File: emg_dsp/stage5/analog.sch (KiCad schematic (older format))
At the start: 37 parts, among them U43 OMNETICS_36

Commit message: working on stage5 already -- will it be tight?
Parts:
- removed TP?: MXA, TP, symbol TP
- removed TP?: MXB, TP, symbol TP
- U26: renamed from U?; footprint (none) -> SC-70-5
- gave numbers to parts that had none: 28
- renumbered C68 to C46, C70 to C49, C76 to C53, L8 to L7, TP174 to TP29, U43 to U24
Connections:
- net E1: now also U24.17 (in16); no longer U24.2 (in1)
- net E10: now also U24.8 (in7); no longer U24.11 (in10)
- net E11: now also U24.7 (in6); no longer U24.12 (in11)
- net E12: now also U24.6 (in5); no longer U24.13 (in12)
- net E13: now also U24.5 (in4); no longer U24.14 (in13)
- net E14: now also U24.4 (in3); no longer U24.15 (in14)
- net E15: now also U24.3 (in2); no longer U24.16 (in15)
- net E16: now also U24.2 (in1); no longer U24.17 (in16)
- net E2: now also U24.16 (in15); no longer U24.3 (in2)
- net E3: now also U24.15 (in14); no longer U24.4 (in3)
- net E4: now also U24.14 (in13); no longer U24.5 (in4)
- net E5: now also U24.13 (in12); no longer U24.6 (in5)
- net E6: now also U24.12 (in11); no longer U24.7 (in6)
- net E7: now also U24.11 (in10); no longer U24.8 (in7)
- net E8: now also U24.10 (in9); no longer U24.9 (in8)
- net E9: now also U24.9 (in8); no longer U24.10 (in9)

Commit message: routing stage5.
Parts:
- removed R45, R51: 3.3k, 0402, symbol R
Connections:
- net E1: now also U25.28 (in15); no longer U25.3 (in0)
- net E10: now also U25.37 (in6); no longer U25.34 (in9)
- net E11: now also U25.38 (in5); no longer U25.33 (in10)
- net E12: now also U25.39 (in4); no longer U25.32 (in11)
- net E13: now also U25.40 (in3); no longer U25.31 (in12)
- net E14: now also U25.1 (in2); no longer U25.30 (in13)
- net E15: now also U25.2 (in1); no longer U25.29 (in14)
- net E16: now also U25.3 (in0); no longer U25.28 (in15)
- net E17: now also U29.28 (in15); no longer U29.3 (in0)
- net E18: now also U29.29 (in14); no longer U29.2 (in1)
- net E19: now also U29.30 (in13); no longer U29.1 (in2)
- net E2: now also U25.29 (in14); no longer U25.2 (in1)
- net E20: now also U29.31 (in12); no longer U29.40 (in3)
- net E21: now also U29.32 (in11); no longer U29.39 (in4)
- net E22: now also U29.33 (in10); no longer U29.38 (in5)
- net E23: now also U29.34 (in9); no longer U29.37 (in6)
- net E24: now also U29.35 (in8); no longer U29.36 (in7)
- net E25: now also U29.36 (in7); no longer U29.35 (in8)
- net E26: now also U29.37 (in6); no longer U29.34 (in9)
- net E27: now also U29.38 (in5); no longer U29.33 (in10)
- net E28: now also U29.39 (in4); no longer U29.32 (in11)
- net E29: now also U29.40 (in3); no longer U29.31 (in12)
- net E3: now also U25.30 (in13); no longer U25.1 (in2)
- net E30: now also U29.1 (in2); no longer U29.30 (in13)
- net E31: now also U29.2 (in1); no longer U29.29 (in14)
- net E32: now also U29.3 (in0); no longer U29.28 (in15)
- net E4: now also U25.31 (in12); no longer U25.40 (in3)
- net E5: now also U25.32 (in11); no longer U25.39 (in4)
- net E6: now also U25.33 (in10); no longer U25.38 (in5)
- net E7: now also U25.34 (in9); no longer U25.37 (in6)
- net E8: now also U25.35 (in8); no longer U25.36 (in7)
- net E9: now also U25.36 (in7); no longer U25.35 (in8)
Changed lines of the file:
@@
-EESchema Schematic File Version 2  date Tue 29 Jun 2010 08:13:18 PM EDT
+EESchema Schematic File Version 2  date Wed 30 Jun 2010 05:27:19 PM EDT
 LIBS:power
 LIBS:device
@@
 Text HLabel 9550 2350 2    60   Input ~ 0
 _reset
+Text Label 7150 1100 0    60   ~ 0
+E32
+Text Label 7150 1200 0    60   ~ 0
+E31
+Text Label 7150 1300 0    60   ~ 0
+E30
+Text Label 7150 1400 0    60   ~ 0
+E29
+Text Label 7150 1500 0    60   ~ 0
+E28
+Text Label 7150 1600 0    60   ~ 0
+E27
+Text Label 7150 1700 0    60   ~ 0
+E26
+Text Label 7150 1800 0    60   ~ 0
+E25
+Text Label 7150 1900 0    60   ~ 0
+E24
+Text Label 7150 2000 0    60   ~ 0
+E23
+Text Label 7150 2100 0    60   ~ 0
+E22
+Text Label 7150 2200 0    60   ~ 0
+E21
+Text Label 7150 2300 0    60   ~ 0
+E20
+Text Label 7150 2400 0    60   ~ 0
+E19
+Text Label 7150 2500 0    60   ~ 0
+E18
 Text Label 7150 2600 0    60   ~ 0
-E32
-Text Label 7150 2500 0    60   ~ 0
-E31
-Text Label 7150 2400 0    60   ~ 0
-E30
-Text Label 7150 2300 0    60   ~ 0
-E29
-Text Label 7150 2200 0    60   ~ 0
-E28
-Text Label 7150 2100 0    60   ~ 0
-E27
-Text Label 7150 2000 0    60   ~ 0
-E26
-Text Label 7150 1900 0    60   ~ 0
-E25
-Text Label 7150 1800 0    60   ~ 0
-E24
-Text Label 7150 1700 0    60   ~ 0
-E23
-Text Label 7150 1600 0    60   ~ 0
-E22
-Text Label 7150 1500 0    60   ~ 0
-E21
-Text Label 7150 1400 0    60   ~ 0
-E20
-Text Label 7150 1300 0    60   ~ 0
-E19
-Text Label 7150 1200 0    60   ~ 0
-E18
-Text Label 7150 1100 0    60   ~ 0
 E17
 $Comp
@@
 F 2 "0402" V 9400 2150 60  0000 C CNN
 	1    9400 1800
-	0    1    1    0
-$EndComp
-$Comp
-L R R51
-U 1 1 4C2A3384
-P 9400 1950
-F 0 "R51" V 9480 1950 50  0000 C CNN
-F 1 "3.3k" V 7500 550 50  0000 C CNN
-F 2 "0402" V 9400 2300 60  0000 C CNN
-	1    9400 1950
 	0    1    1    0
 $EndComp
@@
 $EndComp
 $Comp
-L R R45
-U 1 1 4C2A306D
-P 5450 1950
-F 0 "R45" V 5530 1950 50  0000 C CNN
-F 1 "3.3k" V 3550 550 50  0000 C CNN
-F 2 "0402" V 5450 2300 60  0000 C CNN
-	1    5450 1950
-	0    1    1    0
-$EndComp
-$Comp
 L R R44
 U 1 1 4C2A303D
@@
 	1    0    0    -1
 $EndComp
+Text Label 3200 1100 0    60   ~ 0
+E16
+Text Label 3200 1200 0    60   ~ 0
+E15
+Text Label 3200 1300 0    60   ~ 0
+E14
+Text Label 3200 1400 0    60   ~ 0
+E13
+Text Label 3200 1500 0    60   ~ 0
+E12
+Text Label 3200 1600 0    60   ~ 0
+E11
+Text Label 3200 1700 0    60   ~ 0
+E10
+Text Label 3200 1800 0    60   ~ 0
+E9
+Text Label 3200 1900 0    60   ~ 0
+E8
+Text Label 3200 2000 0    60   ~ 0
+E7
+Text Label 3200 2100 0    60   ~ 0
+E6
+Text Label 3200 2200 0    60   ~ 0
+E5
+Text Label 3200 2300 0    60   ~ 0
+E4
+Text Label 3200 2400 0    60   ~ 0
+E3
+Text Label 3200 2500 0    60   ~ 0
+E2
 Text Label 3200 2600 0    60   ~ 0
-E16
-Text Label 3200 2500 0    60   ~ 0
-E15
-Text Label 3200 2400 0    60   ~ 0
-E14
-Text Label 3200 2300 0    60   ~ 0
-E13
-Text Label 3200 2200 0    60   ~ 0
-E12
-Text Label 3200 2100 0    60   ~ 0
-E11
-Text Label 3200 2000 0    60   ~ 0
-E10
-Text Label 3200 1900 0    60   ~ 0
-E9
-Text Label 3200 1800 0    60   ~ 0
-E8
-Text Label 3200 1700 0    60   ~ 0
-E7
-Text Label 3200 1600 0    60   ~ 0
-E6
-Text Label 3200 1500 0    60   ~ 0
-E5
-Text Label 3200 1400 0    60   ~ 0
-E4
-Text Label 3200 1300 0    60   ~ 0
-E3
-Text Label 3200 1200 0    60   ~ 0
-E2
-Text Label 3200 1100 0    60   ~ 0
 E1
 $Comp

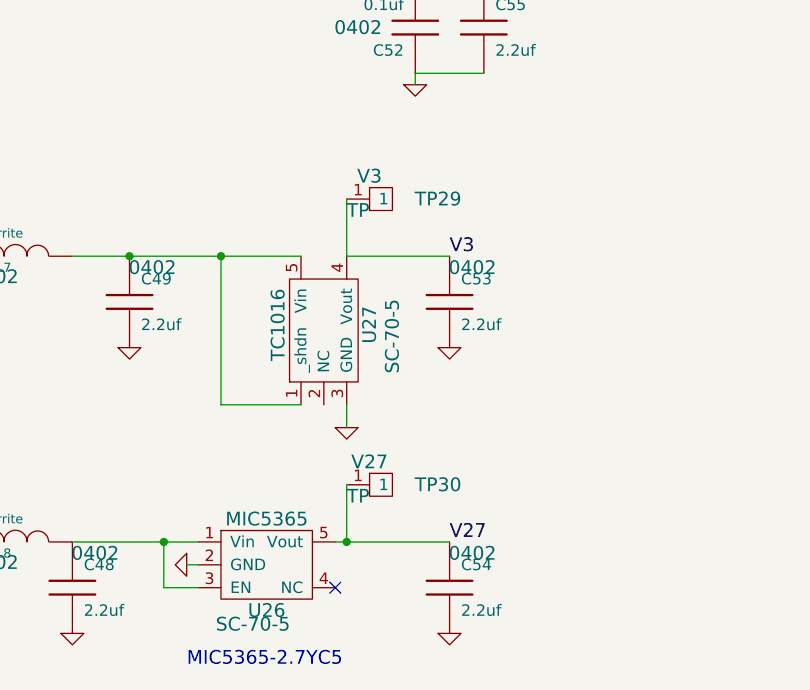
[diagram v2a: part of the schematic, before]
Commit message: board nearing completion - at least with routing! seems to be a bug in the netlist, though -- have to check it out.
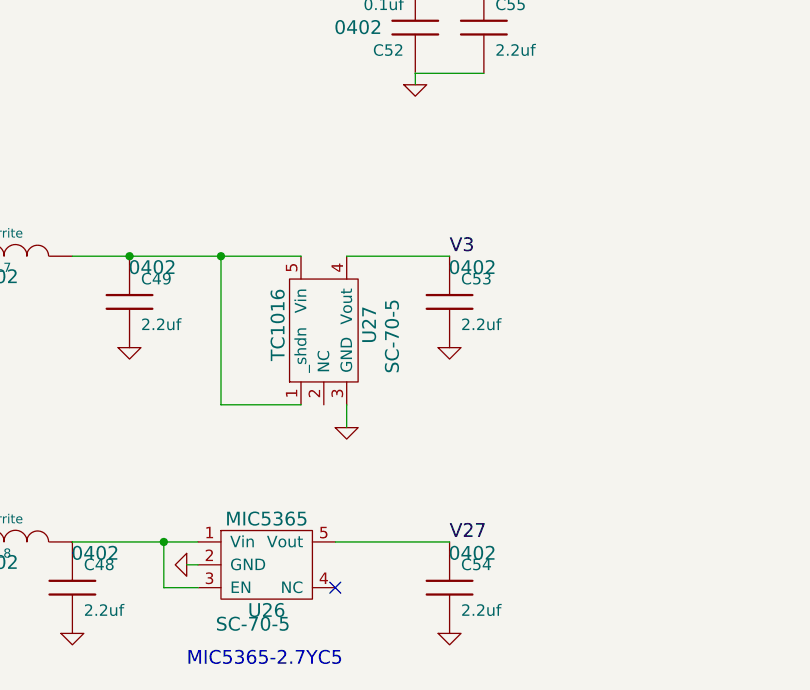
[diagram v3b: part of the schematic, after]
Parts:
- removed TP29: V3, TP, symbol TP
- removed TP30: V27, TP, symbol TP
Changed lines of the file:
@@
-EESchema Schematic File Version 2  date Wed 30 Jun 2010 05:27:19 PM EDT
+EESchema Schematic File Version 2  date Thu 01 Jul 2010 08:06:38 PM EDT
 LIBS:power
 LIBS:device
@@
 Sheet 2 2
 Title "Stage 4 / Copyright 2010 Timothy L Hanson "
-Date "30 jun 2010"
+Date "2 jul 2010"
 Rev ""
 Comp "This design is free: redistribute or modify under the GPL v. 3 or later"
@@
 Wire Wire Line
 	3050 4650 3050 4500
-Connection ~ 4850 5900
 Wire Wire Line
 	4800 5900 5300 5900
@@
 Wire Wire Line
 	5300 4650 4850 4650
-Wire Wire Line
-	4850 4650 4850 4400
-Wire Wire Line
-	4850 5900 4850 5650
 Wire Wire Line
 	3050 5900 3050 5750
@@
 $EndComp
 $Comp
-L GND #PWR0119
+L GND #PWR0121
 U 1 1 4C2A3423
 P 8050 650
-F 0 "#PWR0119" H 8050 650 30  0001 C CNN
+F 0 "#PWR0121" H 8050 650 30  0001 C CNN
 F 1 "GND" H 8050 580 30  0001 C CNN
 	1    8050 650
@@
 $EndComp
 $Comp
-L GND #PWR0120
+L GND #PWR0122
 U 1 1 4C2A338B
 P 7300 2850
-F 0 "#PWR0120" H 7300 2850 30  0001 C CNN
+F 0 "#PWR0122" H 7300 2850 30  0001 C CNN
 F 1 "GND" H 7300 2780 30  0001 C CNN
 	1    7300 2850
@@
 $EndComp
 $Comp
-L GND #PWR0121
+L GND #PWR0123
 U 1 1 4C2A338A
 P 8850 3000
-F 0 "#PWR0121" H 8850 3000 30  0001 C CNN
+F 0 "#PWR0123" H 8850 3000 30  0001 C CNN
 F 1 "GND" H 8850 2930 30  0001 C CNN
 	1    8850 3000
@@
 $EndComp
 $Comp
-L GND #PWR0122
+L GND #PWR0124
 U 1 1 4C2A3388
 P 9300 3050
-F 0 "#PWR0122" H 9300 3050 30  0001 C CNN
+F 0 "#PWR0124" H 9300 3050 30  0001 C CNN
 F 1 "GND" H 9300 2980 30  0001 C CNN
 	1    9300 3050
@@
 $EndComp
 $Comp
-L GND #PWR0123
+L GND #PWR0125
 U 1 1 4C2A3386
 P 9100 3900
-F 0 "#PWR0123" H 9100 3900 30  0001 C CNN
+F 0 "#PWR0125" H 9100 3900 30  0001 C CNN
 F 1 "GND" H 9100 3830 30  0001 C CNN
 	1    9100 3900
@@
 $EndComp
 $Comp
-L GND #PWR0124
+L GND #PWR0126
 U 1 1 4C2A3382
 P 9650 1800
-F 0 "#PWR0124" H 9650 1800 30  0001 C CNN
+F 0 "#PWR0126" H 9650 1800 30  0001 C CNN
 F 1 "GND" H 9650 1730 30  0001 C CNN
 	1    9650 1800
@@
 $EndComp
 $Comp
-L GND #PWR0125
+L GND #PWR0127
 U 1 1 4C2A3381
 P 9650 1950
-F 0 "#PWR0125" H 9650 1950 30  0001 C CNN
+F 0 "#PWR0127" H 9650 1950 30  0001 C CNN
 F 1 "GND" H 9650 1880 30  0001 C CNN
 	1    9650 1950
@@
 $EndComp
 $Comp
-L GND #PWR0126
+L GND #PWR0128
 U 1 1 4C2A337F
 P 9650 2100
-F 0 "#PWR0126" H 9650 2100 30  0001 C CNN
+F 0 "#PWR0128" H 9650 2100 30  0001 C CNN
 F 1 "GND" H 9650 2030 30  0001 C CNN
 	1    9650 2100
@@
 $EndComp
 $Comp
-L GND #PWR0127
+L GND #PWR0129
 U 1 1 4C2A337C
 P 8900 1800
-F 0 "#PWR0127" H 8900 1800 30  0001 C CNN
+F 0 "#PWR0129" H 8900 1800 30  0001 C CNN
 F 1 "GND" H 8900 1730 30  0001 C CNN
 	1    8900 1800
@@
 $EndComp
 $Comp
-L GND #PWR0128
+L GND #PWR0130
 U 1 1 4C2A337B
 P 8900 1250
-F 0 "#PWR0128" H 8900 1250 30  0001 C CNN
+F 0 "#PWR0130" H 8900 1250 30  0001 C CNN
 F 1 "GND" H 8900 1180 30  0001 C CNN
 	1    8900 1250
@@
 V3
 $Comp
-L GND #PWR0129
+L GND #PWR0131
 U 1 1 4C2A337A
 P 8900 2350
-F 0 "#PWR0129" H 8900 2350 30  0001 C CNN
+F 0 "#PWR0131" H 8900 2350 30  0001 C CNN
 F 1 "GND" H 8900 2280 30  0001 C CNN
 	1    8900 2350
@@
 $EndComp
 $Comp
-L GND #PWR0130
+L GND #PWR0132
 U 1 1 4C2A3379
 P 8100 3300
-F 0 "#PWR0130" H 8100 3300 30  0001 C CNN
+F 0 "#PWR0132" H 8100 3300 30  0001 C CNN
 F 1 "GND" H 8100 3230 30  0001 C CNN
 	1    8100 3300
@@
 NoConn ~ 3950 3100
 $Comp
-L GND #PWR0131
+L GND #PWR0133
 U 1 1 4C2A32DF
 P 4100 650
-F 0 "#PWR0131" H 4100 650 30  0001 C CNN
+F 0 "#PWR0133" H 4100 650 30  0001 C CNN
 F 1 "GND" H 4100 580 30  0001 C CNN
 	1    4100 650
@@
 $EndComp
 $Comp
-L GND #PWR0132
+L GND #PWR0134
 U 1 1 4C2A32D7
 P 4150 3300
-F 0 "#PWR0132" H 4150 3300 30  0001 C CNN
+F 0 "#PWR0134" H 4150 3300 30  0001 C CNN
 F 1 "GND" H 4150 3230 30  0001 C CNN
 	1    4150 3300
@@
 $EndComp
 $Comp
-L GND #PWR0133
+L GND #PWR0135
 U 1 1 4C2A32BF
 P 4950 2350
-F 0 "#PWR0133" H 4950 2350 30  0001 C CNN
+F 0 "#PWR0135" H 4950 2350 30  0001 C CNN
 F 1 "GND" H 4950 2280 30  0001 C CNN
 	1    4950 2350
@@
 V3
 $Comp
-L GND #PWR0134
+L GND #PWR0136
 U 1 1 4C2A3286
 P 4950 1250
-F 0 "#PWR0134" H 4950 1250 30  0001 C CNN
+F 0 "#PWR0136" H 4950 1250 30  0001 C CNN
 F 1 "GND" H 4950 1180 30  0001 C CNN
 	1    4950 1250
@@
 $EndComp
 $Comp
-L GND #PWR0135
+L GND #PWR0137
 U 1 1 4C2A3267
 P 4950 1800
-F 0 "#PWR0135" H 4950 1800 30  0001 C CNN
+F 0 "#PWR0137" H 4950 1800 30  0001 C CNN
 F 1 "GND" H 4950 1730 30  0001 C CNN
 	1    4950 1800
@@
 $EndComp
 $Comp
-L GND #PWR0136
+L GND #PWR0138
 U 1 1 4C2A3090
 P 5700 2100
-F 0 "#PWR0136" H 5700 2100 30  0001 C CNN
+F 0 "#PWR0138" H 5700 2100 30  0001 C CNN
 F 1 "GND" H 5700 2030 30  0001 C CNN
 	1    5700 2100
@@
 $EndComp
 $Comp
-L GND #PWR0137
+L GND #PWR0139
 U 1 1 4C2A3089
 P 5700 1950
-F 0 "#PWR0137" H 5700 1950 30  0001 C CNN
+F 0 "#PWR0139" H 5700 1950 30  0001 C CNN
 F 1 "GND" H 5700 1880 30  0001 C CNN
 	1    5700 1950
@@
 $EndComp
 $Comp
-L GND #PWR0138
+L GND #PWR0140
 U 1 1 4C2A3084
 P 5700 1800
-F 0 "#PWR0138" H 5700 1800 30  0001 C CNN
+F 0 "#PWR0140" H 5700 1800 30  0001 C CNN
 F 1 "GND" H 5700 1730 30  0001 C CNN
 	1    5700 1800
@@
 V27
 $Comp
-L VDD #PWR0139
+L VDD #PWR0141
 U 1 1 4C2A2EC5
 P 3050 5750
-F 0 "#PWR0139" H 3050 5850 30  0001 C CNN
+F 0 "#PWR0141" H 3050 5850 30  0001 C CNN
 F 1 "VDD" H 3050 5860 30  0000 C CNN
 	1    3050 5750
@@
 $EndComp
 $Comp
-L GND #PWR0140
+L GND #PWR0142
 U 1 1 4C2A2E8B
 P 5150 3900
-F 0 "#PWR0140" H 5150 3900 30  0001 C CNN
+F 0 "#PWR0142" H 5150 3900 30  0001 C CNN
 F 1 "GND" H 5150 3830 30  0001 C CNN
 	1    5150 3900
@@
 $EndComp
 $Comp
-L GND #PWR0141
+L GND #PWR0143
 U 1 1 4C2A2E11
 P 5350 3050
-F 0 "#PWR0141" H 5350 3050 30  0001 C CNN
+F 0 "#PWR0143" H 5350 3050 30  0001 C CNN
 F 1 "GND" H 5350 2980 30  0001 C CNN
 	1    5350 3050
@@
 $EndComp
 $Comp
-L GND #PWR0142
+L GND #PWR0144
 U 1 1 4C2A2DE8
 P 4900 3000
-F 0 "#PWR0142" H 4900 3000 30  0001 C CNN
+F 0 "#PWR0144" H 4900 3000 30  0001 C CNN
 F 1 "GND" H 4900 2930 30  0001 C CNN
 	1    4900 3000
@@
 $EndComp
 $Comp
-L GND #PWR0143
+L GND #PWR0145
 U 1 1 4C2A2DD8
 P 3350 2850
-F 0 "#PWR0143" H 3350 2850 30  0001 C CNN
+F 0 "#PWR0145" H 3350 2850 30  0001 C CNN
 F 1 "GND" H 3350 2780 30  0001 C CNN
 	1    3350 2850
@@
 $EndComp
 $Comp
-L GND #PWR0144
+L GND #PWR0146
 U 1 1 4C2A2B2E
 P 5300 6300
-F 0 "#PWR0144" H 5300 6300 30  0001 C CNN
+F 0 "#PWR0146" H 5300 6300 30  0001 C CNN
 F 1 "GND" H 5300 6230 30  0001 C CNN
 	1    5300 6300
@@
 $EndComp
 $Comp
-L GND #PWR0145
+L GND #PWR0147
 U 1 1 4C2A2B2C
 P 3650 6300
-F 0 "#PWR0145" H 3650 6300 30  0001 C CNN
+F 0 "#PWR0147" H 3650 6300 30  0001 C CNN
 F 1 "GND" H 3650 6230 30  0001 C CNN
 	1    3650 6300
@@
 $EndComp
 $Comp
-L GND #PWR0146
+L GND #PWR0148
 U 1 1 4C2A2B2B
 P 4150 6000
-F 0 "#PWR0146" H 4150 6000 30  0001 C CNN
+F 0 "#PWR0148" H 4150 6000 30  0001 C CNN
 F 1 "GND" H 4150 5930 30  0001 C CNN
 	1    4150 6000
@@
 $EndComp
 $Comp
-L GND #PWR0147
+L GND #PWR0149
 U 1 1 4C2A2B28
 P 3050 6300
-F 0 "#PWR0147" H 3050 6300 30  0001 C CNN
+F 0 "#PWR0149" H 3050 6300 30  0001 C CNN
 F 1 "GND" H 3050 6230 30  0001 C CNN
 	1    3050 6300
 	-1   0    0    -1
-$EndComp
-$Comp
-L TP TP30
-U 1 1 4C2A2B27
-P 5050 5650
-F 0 "TP30" H 5250 5650 60  0000 C CNN
-F 1 "V27" H 4950 5750 60  0000 C CNN
-F 2 "TP" H 4900 5600 60  0000 C CNN
-	1    5050 5650
-	1    0    0    -1
 $EndComp
 $Comp
@@
 $EndComp
 $Comp
-L VEE #PWR124
+L VEE #PWR126
 U 1 1 4C2A12C9
 P 3050 4500
-F 0 "#PWR124" H 3050 4700 40  0001 C CNN
+F 0 "#PWR126" H 3050 4700 40  0001 C CNN
 F 1 "VEE" H 3050 4650 40  0000 C CNN
 	1    3050 4500
@@
 $EndComp
 $Comp
-L TP TP29
-U 1 1 4B7C6B90
-P 5050 4400
-F 0 "TP29" H 5250 4400 60  0000 C CNN
-F 1 "V3" H 4950 4500 60  0000 C CNN
-F 2 "TP" H 4900 4350 60  0000 C CNN
-	1    5050 4400
-	1    0    0    -1
-$EndComp
-$Comp
-L GND #PWR0148
+L GND #PWR0150
 U 1 1 4B69FA06
 P 3050 5050
-F 0 "#PWR0148" H 3050 5050 30  0001 C CNN
+F 0 "#PWR0150" H 3050 5050 30  0001 C CNN
 F 1 "GND" H 3050 4980 30  0001 C CNN
 	1    3050 5050
@@
 $EndComp
 $Comp
-L GND #PWR0149
+L GND #PWR0151
 U 1 1 4913DE9C
 P 1550 3100
-F 0 "#PWR0149" H 1550 3100 30  0001 C CNN
+F 0 "#PWR0151" H 1550 3100 30  0001 C CNN
 F 1 "GND" H 1550 3030 30  0001 C CNN
 	1    1550 3100
@@
 $EndComp
 $Comp
-L GND #PWR0150
+L GND #PWR0152
 U 1 1 4913DE97
 P 1550 700
-F 0 "#PWR0150" H 1550 700 30  0001 C CNN
+F 0 "#PWR0152" H 1550 700 30  0001 C CNN
 F 1 "GND" H 1550 630 30  0001 C CNN
 	1    1550 700
@@
 V3
 $Comp
-L GND #PWR0151
+L GND #PWR0153
 U 1 1 48FFF0EE
 P 4850 5400
-F 0 "#PWR0151" H 4850 5400 30  0001 C CNN
+F 0 "#PWR0153" H 4850 5400 30  0001 C CNN
 F 1 "GND" H 4850 5330 30  0001 C CNN
 	1    4850 5400
@@
 $EndComp
 $Comp
-L GND #PWR0152
+L GND #PWR0154
 U 1 1 48FFF0D4
 P 3900 5050
-F 0 "#PWR0152" H 3900 5050 30  0001 C CNN
+F 0 "#PWR0154" H 3900 5050 30  0001 C CNN
 F 1 "GND" H 3900 4980 30  0001 C CNN
 	1    3900 5050
@@
 $EndComp
 $Comp
-L GND #PWR0153
+L GND #PWR0155
 U 1 1 48FFF041
 P 5300 5050
-F 0 "#PWR0153" H 5300 5050 30  0001 C CNN
+F 0 "#PWR0155" H 5300 5050 30  0001 C CNN
 F 1 "GND" H 5300 4980 30  0001 C CNN
 	1    5300 5050
